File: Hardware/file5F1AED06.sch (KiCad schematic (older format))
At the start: 15 parts, among them U6 RFPA3800

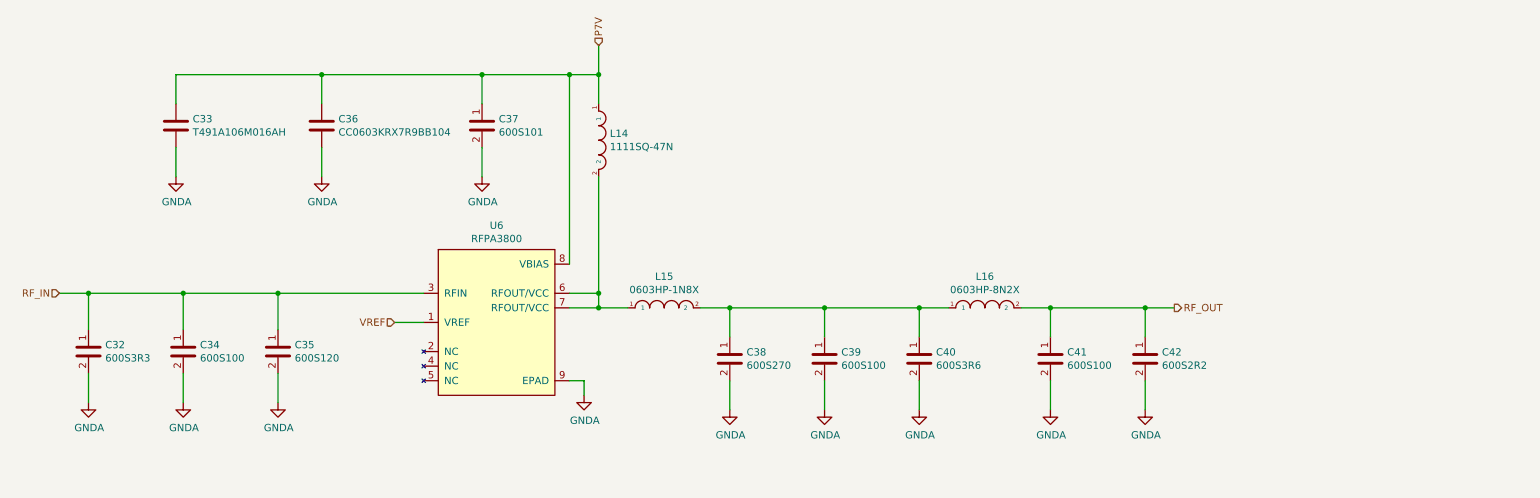
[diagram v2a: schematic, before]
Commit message: Improving LNA simulations and Documentation package. More to come on this one.
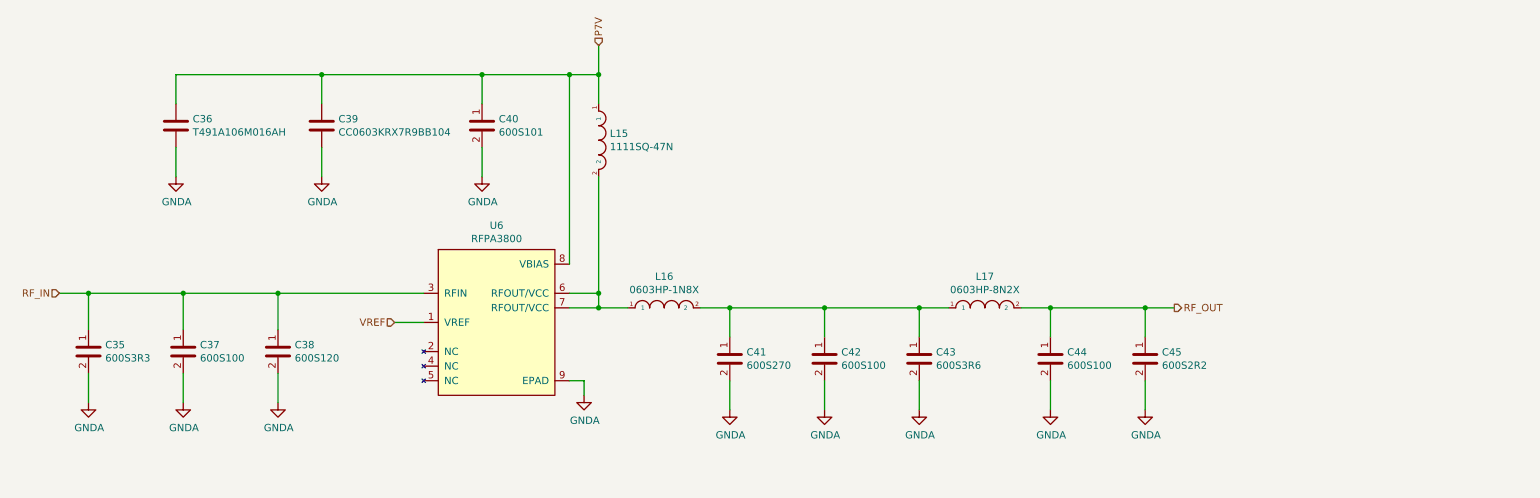
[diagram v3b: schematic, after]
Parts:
- renumbered C32 to C35, C33 to C36, C34 to C37, C35 to C38, C36 to C39, C37 to C40, C38 to C41, C39 to C42, C40 to C43, C41 to C44, C42 to C45, L14 to L15, L15 to L16, L16 to L17
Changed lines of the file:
@@
 $Descr A4 11693 8268
 encoding utf-8
-Sheet 18 24
+Sheet 18 23
 Title ""
 Date ""
@@
 AR Path="/5F04F5B6/5F1D8FAC" Ref="#PWR?"  Part="1"
 AR Path="/5F04F5B6/5F1AED07/5F1D8FAC" Ref="#PWR?"  Part="1"
-AR Path="/5F204DEC/5F205D8E/5F1AED07/5F1D8FAC" Ref="#PWR045"  Part="1"
-F 0 "#PWR045" H 4900 4350 50  0001 C CNN
+AR Path="/5F204DEC/5F205D8E/5F1AED07/5F1D8FAC" Ref="#PWR047"  Part="1"
+F 0 "#PWR047" H 4900 4350 50  0001 C CNN
 F 1 "GNDA" H 4905 4427 50  0000 C CNN
 F 2 "" H 4900 4600 50  0001 C CNN
@@
 AR Path="/5F04F5B6/5F1D8FD9" Ref="#PWR?"  Part="1"
 AR Path="/5F04F5B6/5F1AED07/5F1D8FD9" Ref="#PWR?"  Part="1"
-AR Path="/5F204DEC/5F205D8E/5F1AED07/5F1D8FD9" Ref="#PWR049"  Part="1"
-F 0 "#PWR049" H 8100 4450 50  0001 C CNN
+AR Path="/5F204DEC/5F205D8E/5F1AED07/5F1D8FD9" Ref="#PWR051"  Part="1"
+F 0 "#PWR051" H 8100 4450 50  0001 C CNN
 F 1 "GNDA" H 8105 4527 50  0000 C CNN
 F 2 "" H 8100 4700 50  0001 C CNN
@@
 AR Path="/5F04F5B6/5F1D8FEC" Ref="C?"  Part="1"
 AR Path="/5F04F5B6/5F1AED07/5F1D8FEC" Ref="C?"  Part="1"
-AR Path="/5F204DEC/5F205D8E/5F1AED07/5F1D8FEC" Ref="C37"  Part="1"
-F 0 "C37" H 4315 2796 50  0000 L CNN
+AR Path="/5F204DEC/5F205D8E/5F1AED07/5F1D8FEC" Ref="C40"  Part="1"
+F 0 "C40" H 4315 2796 50  0000 L CNN
 F 1 "600S101" H 4315 2705 50  0000 L CNN
 F 2 "Resistor_SMD:R_0603_1608Metric" H 4250 2850 50  0001 C CNN
@@
 AR Path="/5F04F5B6/5F1D8FF2" Ref="#PWR?"  Part="1"
 AR Path="/5F04F5B6/5F1AED07/5F1D8FF2" Ref="#PWR?"  Part="1"
-AR Path="/5F204DEC/5F205D8E/5F1AED07/5F1D8FF2" Ref="#PWR043"  Part="1"
-F 0 "#PWR043" H 3100 2850 50  0001 C CNN
+AR Path="/5F204DEC/5F205D8E/5F1AED07/5F1D8FF2" Ref="#PWR045"  Part="1"
+F 0 "#PWR045" H 3100 2850 50  0001 C CNN
 F 1 "GNDA" H 3105 2927 50  0000 C CNN
 F 2 "" H 3100 3100 50  0001 C CNN
@@
 AR Path="/5F04F5B6/5F1D8FF9" Ref="#PWR?"  Part="1"
 AR Path="/5F04F5B6/5F1AED07/5F1D8FF9" Ref="#PWR?"  Part="1"
-AR Path="/5F204DEC/5F205D8E/5F1AED07/5F1D8FF9" Ref="#PWR044"  Part="1"
-F 0 "#PWR044" H 4200 2850 50  0001 C CNN
+AR Path="/5F204DEC/5F205D8E/5F1AED07/5F1D8FF9" Ref="#PWR046"  Part="1"
+F 0 "#PWR046" H 4200 2850 50  0001 C CNN
 F 1 "GNDA" H 4205 2927 50  0000 C CNN
 F 2 "" H 4200 3100 50  0001 C CNN
@@
 AR Path="/5F04F5B6/5F1D9008" Ref="C?"  Part="1"
 AR Path="/5F04F5B6/5F1AED07/5F1D9008" Ref="C?"  Part="1"
-AR Path="/5F204DEC/5F205D8E/5F1AED07/5F1D9008" Ref="C36"  Part="1"
-F 0 "C36" H 3215 2796 50  0000 L CNN
+AR Path="/5F204DEC/5F205D8E/5F1AED07/5F1D9008" Ref="C39"  Part="1"
+F 0 "C39" H 3215 2796 50  0000 L CNN
 F 1 "CC0603KRX7R9BB104" H 3215 2705 50  0000 L CNN
 F 2 "Capacitor_SMD:C_0603_1608Metric" H 3138 2600 50  0001 C CNN
@@
 AR Path="/5F04F5B6/5F1D9010" Ref="L?"  Part="1"
 AR Path="/5F04F5B6/5F1AED07/5F1D9010" Ref="L?"  Part="1"
-AR Path="/5F204DEC/5F205D8E/5F1AED07/5F1D9010" Ref="L14"  Part="1"
-F 0 "L14" V 4954 2927 50  0000 L CNN
+AR Path="/5F204DEC/5F205D8E/5F1AED07/5F1D9010" Ref="L15"  Part="1"
+F 0 "L15" V 4954 2927 50  0000 L CNN
 F 1 "1111SQ-47N" V 5045 2927 50  0000 L CNN
 F 2 "Inductor_SMD:L_Coilcraft_1111SQ-47N" H 4750 3000 50  0001 C CNN
@@
 AR Path="/5F04F5B6/5F1D9016" Ref="C?"  Part="1"
 AR Path="/5F04F5B6/5F1AED07/5F1D9016" Ref="C?"  Part="1"
-AR Path="/5F204DEC/5F205D8E/5F1AED07/5F1D9016" Ref="C34"  Part="1"
-F 0 "C34" H 2265 4346 50  0000 L CNN
+AR Path="/5F204DEC/5F205D8E/5F1AED07/5F1D9016" Ref="C37"  Part="1"
+F 0 "C37" H 2265 4346 50  0000 L CNN
 F 1 "600S100" H 2265 4255 50  0000 L CNN
 F 2 "Capacitor_SMD:C_0603_1608Metric" H 2200 4400 50  0001 C CNN
@@
 AR Path="/5F04F5B6/5F1D901C" Ref="C?"  Part="1"
 AR Path="/5F04F5B6/5F1AED07/5F1D901C" Ref="C?"  Part="1"
-AR Path="/5F204DEC/5F205D8E/5F1AED07/5F1D901C" Ref="C35"  Part="1"
-F 0 "C35" H 2915 4346 50  0000 L CNN
+AR Path="/5F204DEC/5F205D8E/5F1AED07/5F1D901C" Ref="C38"  Part="1"
+F 0 "C38" H 2915 4346 50  0000 L CNN
 F 1 "600S120" H 2915 4255 50  0000 L CNN
 F 2 "Capacitor_SMD:C_0603_1608Metric" H 2850 4400 50  0001 C CNN
@@
 AR Path="/5F04F5B6/5F1D9022" Ref="C?"  Part="1"
 AR Path="/5F04F5B6/5F1AED07/5F1D9022" Ref="C?"  Part="1"
-AR Path="/5F204DEC/5F205D8E/5F1AED07/5F1D9022" Ref="C32"  Part="1"
-F 0 "C32" H 1615 4346 50  0000 L CNN
+AR Path="/5F204DEC/5F205D8E/5F1AED07/5F1D9022" Ref="C35"  Part="1"
+F 0 "C35" H 1615 4346 50  0000 L CNN
 F 1 "600S3R3" H 1615 4255 50  0000 L CNN
 F 2 "Capacitor_SMD:C_0603_1608Metric" H 1550 4400 50  0001 C CNN
@@
 RF_IN
 $Comp
-L power:GNDA #PWR039
+L power:GNDA #PWR041
 U 1 1 5F1E2B17
 P 1500 4650
-F 0 "#PWR039" H 1500 4400 50  0001 C CNN
+F 0 "#PWR041" H 1500 4400 50  0001 C CNN
 F 1 "GNDA" H 1505 4477 50  0000 C CNN
 F 2 "" H 1500 4650 50  0001 C CNN
@@
 $EndComp
 $Comp
-L power:GNDA #PWR041
+L power:GNDA #PWR043
 U 1 1 5F1E2D76
 P 2150 4650
-F 0 "#PWR041" H 2150 4400 50  0001 C CNN
+F 0 "#PWR043" H 2150 4400 50  0001 C CNN
 F 1 "GNDA" H 2155 4477 50  0000 C CNN
 F 2 "" H 2150 4650 50  0001 C CNN
@@
 $EndComp
 $Comp
-L power:GNDA #PWR042
+L power:GNDA #PWR044
 U 1 1 5F1E3182
 P 2800 4650
-F 0 "#PWR042" H 2800 4400 50  0001 C CNN
+F 0 "#PWR044" H 2800 4400 50  0001 C CNN
 F 1 "GNDA" H 2805 4477 50  0000 C CNN
 F 2 "" H 2800 4650 50  0001 C CNN
@@
 	8100 4700 8100 4500
 $Comp
-L Coilcraft:0603HP-1N8X L15
+L Coilcraft:0603HP-1N8X L16
 U 1 1 5F1EAA6E
 P 5450 4000
-F 0 "L15" H 5450 4215 50  0000 C CNN
+F 0 "L16" H 5450 4215 50  0000 C CNN
 F 1 "0603HP-1N8X" H 5450 4124 50  0000 C CNN
 F 2 "Inductor_SMD:L_0603_1608Metric" H 5200 4150 50  0001 C CNN
@@
 $EndComp
 $Comp
-L ATC:600S270 C38
+L ATC:600S270 C41
 U 1 1 5F1EB80A
 P 5900 4350
-F 0 "C38" H 6015 4396 50  0000 L CNN
+F 0 "C41" H 6015 4396 50  0000 L CNN
 F 1 "600S270" H 6015 4305 50  0000 L CNN
 F 2 "Capacitor_SMD:C_0603_1608Metric" H 5950 4450 50  0001 C CNN
@@
 $EndComp
 $Comp
-L ATC:600S100 C39
+L ATC:600S100 C42
 U 1 1 5F1EBBE5
 P 6550 4350
-F 0 "C39" H 6665 4396 50  0000 L CNN
+F 0 "C42" H 6665 4396 50  0000 L CNN
 F 1 "600S100" H 6665 4305 50  0000 L CNN
 F 2 "Capacitor_SMD:C_0603_1608Metric" H 6600 4450 50  0001 C CNN
@@
 $EndComp
 $Comp
-L ATC:600S3R6 C40
+L ATC:600S3R6 C43
 U 1 1 5F1EBFC8
 P 7200 4350
-F 0 "C40" H 7315 4396 50  0000 L CNN
+F 0 "C43" H 7315 4396 50  0000 L CNN
 F 1 "600S3R6" H 7315 4305 50  0000 L CNN
 F 2 "Capacitor_SMD:C_0603_1608Metric" H 7250 4450 50  0001 C CNN
@@
 $EndComp
 $Comp
-L Coilcraft:0603HP-8N2X L16
+L Coilcraft:0603HP-8N2X L17
 U 1 1 5F1EC368
 P 7650 4000
-F 0 "L16" H 7650 4215 50  0000 C CNN
+F 0 "L17" H 7650 4215 50  0000 C CNN
 F 1 "0603HP-8N2X" H 7650 4124 50  0000 C CNN
 F 2 "Inductor_SMD:L_0603_1608Metric" H 7400 4150 50  0001 C CNN
@@
 $EndComp
 $Comp
-L ATC:600S100 C41
+L ATC:600S100 C44
 U 1 1 5F1EC703
 P 8100 4350
-F 0 "C41" H 8215 4396 50  0000 L CNN
+F 0 "C44" H 8215 4396 50  0000 L CNN
 F 1 "600S100" H 8215 4305 50  0000 L CNN
 F 2 "Capacitor_SMD:C_0603_1608Metric" H 8150 4450 50  0001 C CNN
@@
 $EndComp
 $Comp
-L ATC:600S2R2 C42
+L ATC:600S2R2 C45
 U 1 1 5F1ECAB0
 P 8750 4350
-F 0 "C42" H 8865 4396 50  0000 L CNN
+F 0 "C45" H 8865 4396 50  0000 L CNN
 F 1 "600S2R2" H 8865 4305 50  0000 L CNN
 F 2 "Capacitor_SMD:C_0603_1608Metric" H 8800 4450 50  0001 C CNN
@@
 AR Path="/5F04F5B6/5F1F33B9" Ref="#PWR?"  Part="1"
 AR Path="/5F04F5B6/5F1AED07/5F1F33B9" Ref="#PWR?"  Part="1"
-AR Path="/5F204DEC/5F205D8E/5F1AED07/5F1F33B9" Ref="#PWR048"  Part="1"
-F 0 "#PWR048" H 7200 4450 50  0001 C CNN
+AR Path="/5F204DEC/5F205D8E/5F1AED07/5F1F33B9" Ref="#PWR050"  Part="1"
+F 0 "#PWR050" H 7200 4450 50  0001 C CNN
 F 1 "GNDA" H 7205 4527 50  0000 C CNN
 F 2 "" H 7200 4700 50  0001 C CNN
@@
 AR Path="/5F04F5B6/5F1F3A81" Ref="#PWR?"  Part="1"
 AR Path="/5F04F5B6/5F1AED07/5F1F3A81" Ref="#PWR?"  Part="1"
-AR Path="/5F204DEC/5F205D8E/5F1AED07/5F1F3A81" Ref="#PWR047"  Part="1"
-F 0 "#PWR047" H 6550 4450 50  0001 C CNN
+AR Path="/5F204DEC/5F205D8E/5F1AED07/5F1F3A81" Ref="#PWR049"  Part="1"
+F 0 "#PWR049" H 6550 4450 50  0001 C CNN
 F 1 "GNDA" H 6555 4527 50  0000 C CNN
 F 2 "" H 6550 4700 50  0001 C CNN
@@
 AR Path="/5F04F5B6/5F1F436D" Ref="#PWR?"  Part="1"
 AR Path="/5F04F5B6/5F1AED07/5F1F436D" Ref="#PWR?"  Part="1"
-AR Path="/5F204DEC/5F205D8E/5F1AED07/5F1F436D" Ref="#PWR046"  Part="1"
-F 0 "#PWR046" H 5900 4450 50  0001 C CNN
+AR Path="/5F204DEC/5F205D8E/5F1AED07/5F1F436D" Ref="#PWR048"  Part="1"
+F 0 "#PWR048" H 5900 4450 50  0001 C CNN
 F 1 "GNDA" H 5905 4527 50  0000 C CNN
 F 2 "" H 5900 4700 50  0001 C CNN
@@
 AR Path="/5F04F5B6/5F1F4C55" Ref="#PWR?"  Part="1"
 AR Path="/5F04F5B6/5F1AED07/5F1F4C55" Ref="#PWR?"  Part="1"
-AR Path="/5F204DEC/5F205D8E/5F1AED07/5F1F4C55" Ref="#PWR050"  Part="1"
-F 0 "#PWR050" H 8750 4450 50  0001 C CNN
+AR Path="/5F204DEC/5F205D8E/5F1AED07/5F1F4C55" Ref="#PWR052"  Part="1"
+F 0 "#PWR052" H 8750 4450 50  0001 C CNN
 F 1 "GNDA" H 8755 4527 50  0000 C CNN
 F 2 "" H 8750 4700 50  0001 C CNN
@@
 VREF
 $Comp
-L Kemet:T491A106M016AH C33
+L Kemet:T491A106M016AH C36
 U 1 1 5F2FD57C
 P 2100 2750
-F 0 "C33" H 2215 2796 50  0000 L CNN
+F 0 "C36" H 2215 2796 50  0000 L CNN
 F 1 "T491A106M016AH" H 2215 2705 50  0000 L CNN
 F 2 "Capacitor_SMD:C_1206_3216Metric" H 2138 2600 50  0001 C CNN
@@
 AR Path="/5F04F5B6/5F2FE672" Ref="#PWR?"  Part="1"
 AR Path="/5F04F5B6/5F1AED07/5F2FE672" Ref="#PWR?"  Part="1"
-AR Path="/5F204DEC/5F205D8E/5F1AED07/5F2FE672" Ref="#PWR040"  Part="1"
-F 0 "#PWR040" H 2100 2850 50  0001 C CNN
+AR Path="/5F204DEC/5F205D8E/5F1AED07/5F2FE672" Ref="#PWR042"  Part="1"
+F 0 "#PWR042" H 2100 2850 50  0001 C CNN
 F 1 "GNDA" H 2105 2927 50  0000 C CNN
 F 2 "" H 2100 3100 50  0001 C CNN
